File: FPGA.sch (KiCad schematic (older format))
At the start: 56 parts, among them J1 Conn_02x07_Odd_Even, J2 26642801RP2, U3 XC7A100T-FTG256, U4 S25FL1, U5 SiT2024B, U6 AS6C1616

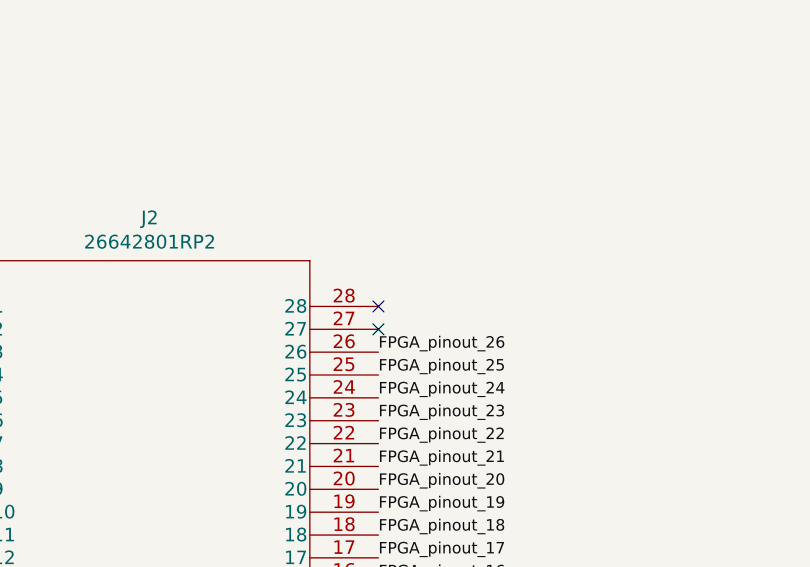
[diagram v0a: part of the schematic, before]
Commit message: Partially route FPGA
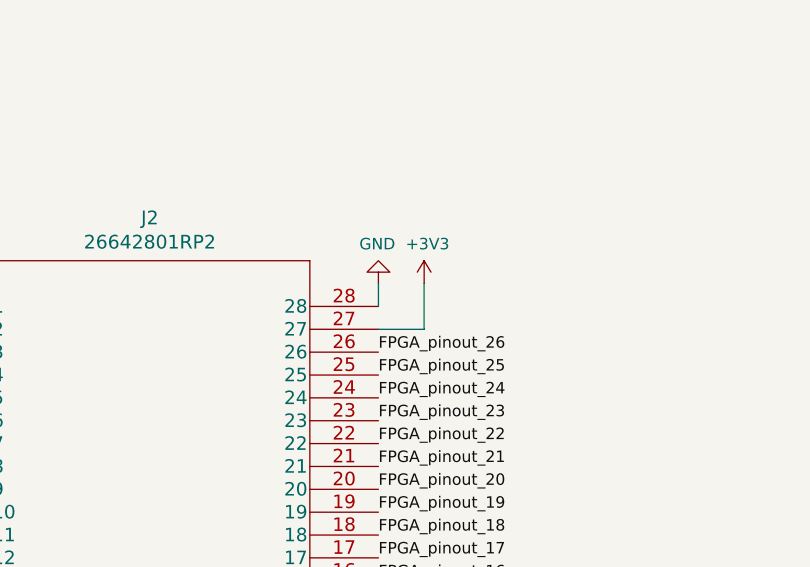
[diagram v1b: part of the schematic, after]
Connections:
- net +3V3: now also J2.27
- net GND: now also J2.28
- no-connect marks 90 -> 88
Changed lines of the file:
@@
 Text Label 5850 9000 0    50   ~ 0
 FPGA_pinout_26
-NoConn ~ 5850 8800
-NoConn ~ 5850 8900
 Wire Wire Line
 	5400 4000 6900 4000
@@
 Text Notes -400 7450 2    50   ~ 0
 Vccint
+$Comp
+L power:GND #PWR0172
+U 1 1 5D9DC146
+P 5850 8700
+F 0 "#PWR0172" H 5850 8450 50  0001 C CNN
+F 1 "GND" H 5855 8527 50  0000 C CNN
+F 2 "" H 5850 8700 50  0001 C CNN
+F 3 "" H 5850 8700 50  0001 C CNN
+	1    5850 8700
+	-1   0    0    1
+$EndComp
+$Comp
+L power:+3V3 #PWR0181
+U 1 1 5D9DC78C
+P 6050 8700
+F 0 "#PWR0181" H 6050 8550 50  0001 C CNN
+F 1 "+3V3" H 6065 8873 50  0000 C CNN
+F 2 "" H 6050 8700 50  0001 C CNN
+F 3 "" H 6050 8700 50  0001 C CNN
+	1    6050 8700
+	1    0    0    -1
+$EndComp
+Wire Wire Line
+	5850 8800 5850 8700
+Wire Wire Line
+	6050 8700 6050 8900
+Wire Wire Line
+	6050 8900 5850 8900
 $EndSCHEMATC

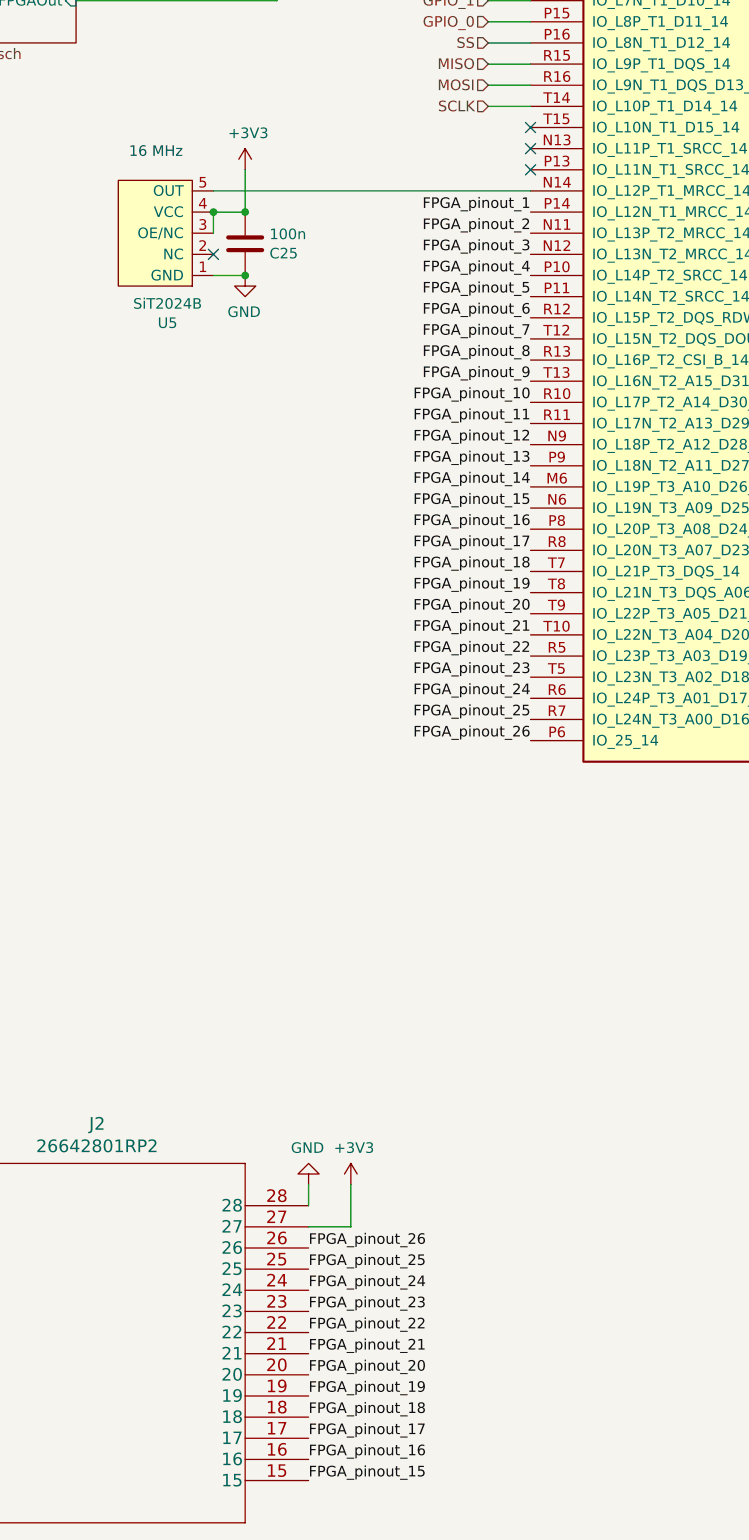
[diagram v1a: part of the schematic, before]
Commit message: Partially route FPGA pinout
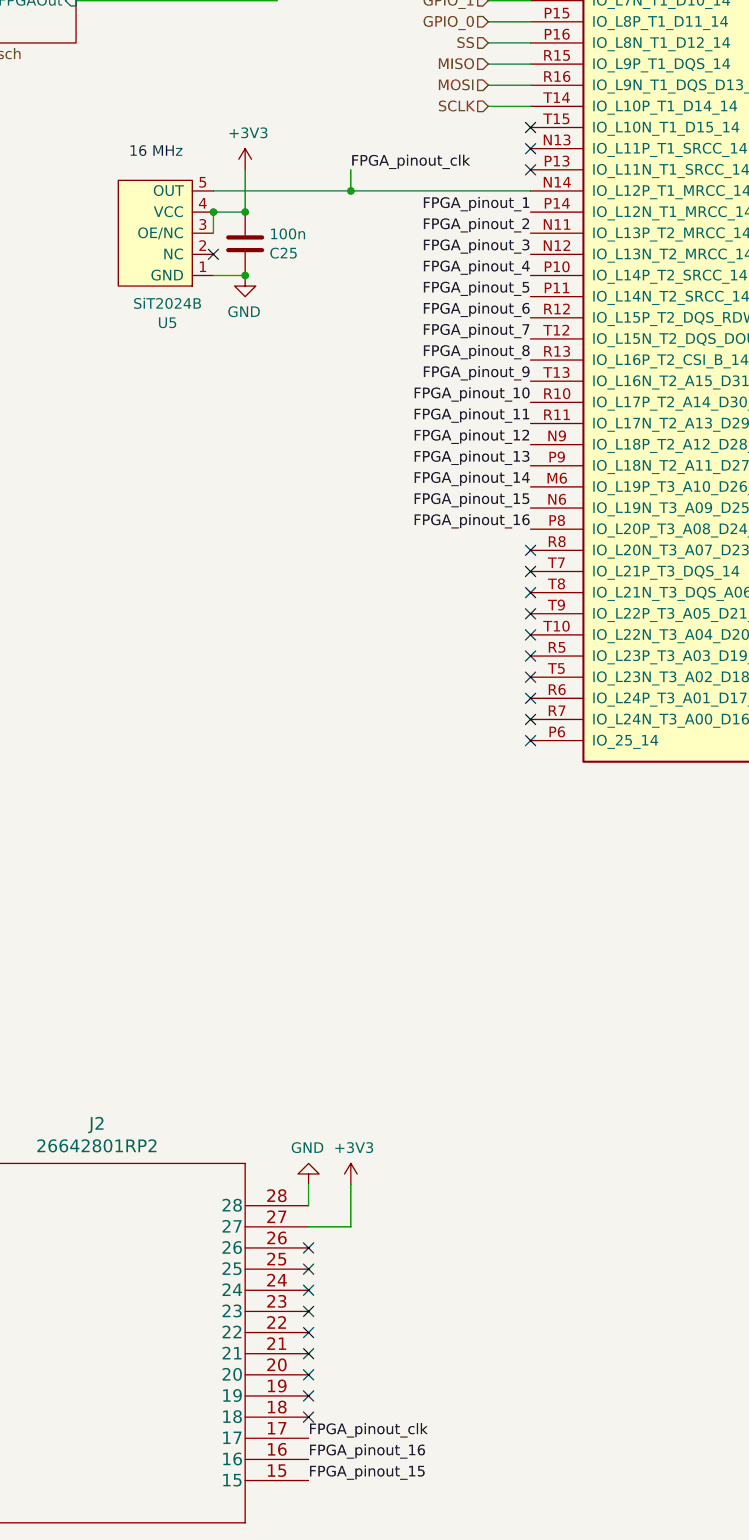
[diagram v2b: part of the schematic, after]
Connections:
- net FPGA_pinout_clk: now reaches U3.N14 (IO_L12P_T1_MRCC_14), U5.5 (OUT)
- net FPGA_pinout_clk: now also J2.17
- net FPGA_pinout_17: no longer names the net of U3.R8 (IO_L20N_T3_A07_D23_14)
- net FPGA_pinout_17: no longer J2.17
- net FPGA_pinout_18: no longer names the net of U3.T7 (IO_L21P_T3_DQS_14)
- net FPGA_pinout_18: no longer J2.18
- net FPGA_pinout_19: no longer names the net of U3.T8 (IO_L21N_T3_DQS_A06_D22_14)
- net FPGA_pinout_19: no longer J2.19
- net FPGA_pinout_20: no longer names the net of U3.T9 (IO_L22P_T3_A05_D21_14)
- net FPGA_pinout_20: no longer J2.20
- net FPGA_pinout_21: no longer names the net of U3.T10 (IO_L22N_T3_A04_D20_14)
- net FPGA_pinout_21: no longer J2.21
- net FPGA_pinout_22: no longer names the net of U3.R5 (IO_L23P_T3_A03_D19_14)
- net FPGA_pinout_22: no longer J2.22
- net FPGA_pinout_23: no longer names the net of U3.T5 (IO_L23N_T3_A02_D18_14)
- net FPGA_pinout_23: no longer J2.23
- net FPGA_pinout_24: no longer names the net of U3.R6 (IO_L24P_T3_A01_D17_14)
- net FPGA_pinout_24: no longer J2.24
- net FPGA_pinout_25: no longer names the net of U3.R7 (IO_L24N_T3_A00_D16_14)
- net FPGA_pinout_25: no longer J2.25
- net FPGA_pinout_26: no longer names the net of U3.P6 (IO_25_14)
- net FPGA_pinout_26: no longer J2.26
- no-connect marks 88 -> 107
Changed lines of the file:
@@
 Wire Wire Line
 	6900 3200 6700 3200
-$Comp
-L pin_header:26642801RP2 J2
-U 1 1 5F44891F
-P 3850 8800
-F 0 "J2" H 4850 9187 60  0000 C CNN
-F 1 "26642801RP2" H 4850 9081 60  0000 C CNN
-F 2 "Connector_PinHeader_2.54mm:PinHeader_2x14_P2.54mm_Vertical" H 4850 9040 60  0001 C CNN
-F 3 "" H 3850 8800 60  0000 C CNN
-	1    3850 8800
-	1    0    0    -1
-$EndComp
 Text Label 6900 4100 2    50   ~ 0
 FPGA_pinout_1
@@
 Text Label 6900 5600 2    50   ~ 0
 FPGA_pinout_16
-Text Label 6900 5700 2    50   ~ 0
-FPGA_pinout_17
-Text Label 6900 5800 2    50   ~ 0
-FPGA_pinout_18
-Text Label 6900 5900 2    50   ~ 0
-FPGA_pinout_19
-Text Label 6900 6000 2    50   ~ 0
-FPGA_pinout_20
-Text Label 6900 6100 2    50   ~ 0
-FPGA_pinout_21
-Text Label 6900 6200 2    50   ~ 0
-FPGA_pinout_22
-Text Label 6900 6300 2    50   ~ 0
-FPGA_pinout_23
-Text Label 6900 6400 2    50   ~ 0
-FPGA_pinout_24
-Text Label 6900 6500 2    50   ~ 0
-FPGA_pinout_25
-Text Label 6900 6600 2    50   ~ 0
-FPGA_pinout_26
-Text Label 3850 8800 2    50   ~ 0
-FPGA_pinout_1
-Text Label 3850 8900 2    50   ~ 0
-FPGA_pinout_2
-Text Label 3850 9000 2    50   ~ 0
-FPGA_pinout_3
-Text Label 3850 9100 2    50   ~ 0
-FPGA_pinout_4
-Text Label 3850 9200 2    50   ~ 0
-FPGA_pinout_5
-Text Label 3850 9300 2    50   ~ 0
-FPGA_pinout_6
-Text Label 3850 9400 2    50   ~ 0
-FPGA_pinout_7
-Text Label 3850 9500 2    50   ~ 0
-FPGA_pinout_8
-Text Label 3850 9600 2    50   ~ 0
-FPGA_pinout_9
-Text Label 3850 9700 2    50   ~ 0
-FPGA_pinout_10
-Text Label 3850 9800 2    50   ~ 0
-FPGA_pinout_11
-Text Label 3850 9900 2    50   ~ 0
-FPGA_pinout_12
-Text Label 3850 10000 2    50   ~ 0
-FPGA_pinout_13
-Text Label 3850 10100 2    50   ~ 0
-FPGA_pinout_14
-Text Label 5850 10100 0    50   ~ 0
-FPGA_pinout_15
-Text Label 5850 10000 0    50   ~ 0
-FPGA_pinout_16
-Text Label 5850 9900 0    50   ~ 0
-FPGA_pinout_17
-Text Label 5850 9800 0    50   ~ 0
-FPGA_pinout_18
-Text Label 5850 9700 0    50   ~ 0
-FPGA_pinout_19
-Text Label 5850 9600 0    50   ~ 0
-FPGA_pinout_20
-Text Label 5850 9500 0    50   ~ 0
-FPGA_pinout_21
-Text Label 5850 9400 0    50   ~ 0
-FPGA_pinout_22
-Text Label 5850 9300 0    50   ~ 0
-FPGA_pinout_23
-Text Label 5850 9200 0    50   ~ 0
-FPGA_pinout_24
-Text Label 5850 9100 0    50   ~ 0
-FPGA_pinout_25
-Text Label 5850 9000 0    50   ~ 0
-FPGA_pinout_26
-Wire Wire Line
-	5400 4000 6900 4000
+Wire Wire Line
+	5400 4000 6050 4000
 Text Notes -300 6200 2    50   ~ 0
 Vccbram
@@
 Text Notes -400 7450 2    50   ~ 0
 Vccint
+Wire Wire Line
+	6050 8900 5850 8900
+Wire Wire Line
+	6050 8700 6050 8900
+Wire Wire Line
+	5850 8800 5850 8700
+$Comp
+L power:+3V3 #PWR0181
+U 1 1 5D9DC78C
+P 6050 8700
+F 0 "#PWR0181" H 6050 8550 50  0001 C CNN
+F 1 "+3V3" H 6065 8873 50  0000 C CNN
+F 2 "" H 6050 8700 50  0001 C CNN
+F 3 "" H 6050 8700 50  0001 C CNN
+	1    6050 8700
+	1    0    0    -1
+$EndComp
 $Comp
 L power:GND #PWR0172
@@
 $EndComp
 $Comp
-L power:+3V3 #PWR0181
-U 1 1 5D9DC78C
-P 6050 8700
-F 0 "#PWR0181" H 6050 8550 50  0001 C CNN
-F 1 "+3V3" H 6065 8873 50  0000 C CNN
-F 2 "" H 6050 8700 50  0001 C CNN
-F 3 "" H 6050 8700 50  0001 C CNN
-	1    6050 8700
+L pin_header:26642801RP2 J2
+U 1 1 5F44891F
+P 3850 8800
+F 0 "J2" H 4850 9187 60  0000 C CNN
+F 1 "26642801RP2" H 4850 9081 60  0000 C CNN
+F 2 "Connector_PinHeader_2.54mm:PinHeader_2x14_P2.54mm_Vertical" H 4850 9040 60  0001 C CNN
+F 3 "" H 3850 8800 60  0000 C CNN
+	1    3850 8800
 	1    0    0    -1
 $EndComp
-Wire Wire Line
-	5850 8800 5850 8700
-Wire Wire Line
-	6050 8700 6050 8900
-Wire Wire Line
-	6050 8900 5850 8900
+Text Label 3850 9500 2    50   ~ 0
+FPGA_pinout_8
+Text Label 3850 9400 2    50   ~ 0
+FPGA_pinout_7
+Text Label 3850 9300 2    50   ~ 0
+FPGA_pinout_6
+Text Label 3850 9200 2    50   ~ 0
+FPGA_pinout_5
+Text Label 3850 9100 2    50   ~ 0
+FPGA_pinout_4
+Text Label 3850 9000 2    50   ~ 0
+FPGA_pinout_3
+Text Label 3850 8900 2    50   ~ 0
+FPGA_pinout_2
+Text Label 3850 8800 2    50   ~ 0
+FPGA_pinout_1
+Text Label 3850 10100 2    50   ~ 0
+FPGA_pinout_14
+Text Label 3850 10000 2    50   ~ 0
+FPGA_pinout_13
+Text Label 3850 9900 2    50   ~ 0
+FPGA_pinout_12
+Text Label 3850 9800 2    50   ~ 0
+FPGA_pinout_11
+Text Label 3850 9700 2    50   ~ 0
+FPGA_pinout_10
+Text Label 3850 9600 2    50   ~ 0
+FPGA_pinout_9
+Text Label 5850 10000 0    50   ~ 0
+FPGA_pinout_16
+Text Label 5850 10100 0    50   ~ 0
+FPGA_pinout_15
+Text Label 5850 9900 0    50   ~ 0
+FPGA_pinout_clk
+NoConn ~ 5850 9000
+NoConn ~ 5850 9100
+NoConn ~ 5850 9200
+NoConn ~ 5850 9300
+NoConn ~ 5850 9400
+NoConn ~ 5850 9500
+NoConn ~ 5850 9600
+NoConn ~ 5850 9700
+NoConn ~ 5850 9800
+NoConn ~ 6900 5700
+NoConn ~ 6900 5800
+NoConn ~ 6900 5900
+NoConn ~ 6900 6000
+NoConn ~ 6900 6100
+NoConn ~ 6900 6200
+NoConn ~ 6900 6300
+NoConn ~ 6900 6400
+NoConn ~ 6900 6500
+NoConn ~ 6900 6600
+Text Label 6050 3900 0    50   ~ 0
+FPGA_pinout_clk
+Wire Wire Line
+	6050 3900 6050 4000
+Connection ~ 6050 4000
+Wire Wire Line
+	6050 4000 6900 4000
 $EndSCHEMATC

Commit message: Finish PCB wiring
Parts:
- removed C48: 47u, Capacitor_SMD:C_1206_3216Metric_Pad1.42x1.75mm_HandSolder, symbol Device:C
- removed C50, C52: 4.7u, Capacitor_SMD:C_1206_3216Metric_Pad1.42x1.75mm_HandSolder, symbol Device:C
- removed C54, C56, C58, C60: 0.47u, Capacitor_SMD:C_1206_3216Metric_Pad1.42x1.75mm_HandSolder, symbol Device:C
- removed C63: 100n, Capacitor_SMD:C_1206_3216Metric_Pad1.42x1.75mm_HandSolder, symbol Device:C
- removed U6: AS6C1616, Package_SO:TSOP-I-48_18.4x12mm_P0.5mm, symbol Memory_RAM:AS6C1616
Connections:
- net +3V3: no longer U3.A6 (VCCO_35), U3.B3 (VCCO_35), U3.D7 (VCCO_35), U3.E4 (VCCO_35), U3.F1 (VCCO_35), U3.J2 (VCCO_35)
- net GND: now also U3.A6 (VCCO_35), U3.B3 (VCCO_35), U3.D7 (VCCO_35), U3.E4 (VCCO_35), U3.F1 (VCCO_35), U3.J2 (VCCO_35)
- net FPGA_pinout_clk: no longer names the net of U3.N14 (IO_L12P_T1_MRCC_14), U5.5 (OUT)
- net FPGA_pinout_clk: no longer J2.17
- net SRAM_a0: no longer names the net of U3.A2 (IO_L8N_T1_AD14N_35)
- net SRAM_a1: no longer names the net of U3.C1 (IO_L9P_T1_DQS_AD7P_35)
- net SRAM_a10: no longer names the net of U3.E5 (IO_L13N_T2_MRCC_35)
- net SRAM_a11: no longer names the net of U3.F4 (IO_L14P_T2_SRCC_35)
- net SRAM_a12: no longer names the net of U3.F3 (IO_L14N_T2_SRCC_35)
- net SRAM_a13: no longer names the net of U3.F2 (IO_L15P_T2_DQS_35)
- net SRAM_a14: no longer names the net of U3.E1 (IO_L15N_T2_DQS_35)
- net SRAM_a15: no longer names the net of U3.G5 (IO_L16P_T2_35)
- net SRAM_a16: no longer names the net of U3.G4 (IO_L16N_T2_35)
- net SRAM_a17: no longer names the net of U3.G2 (IO_L17P_T2_35)
- net SRAM_a18: no longer names the net of U3.G1 (IO_L17N_T2_35)
- net SRAM_a19: no longer names the net of U3.H5 (IO_L18P_T2_35)
- net SRAM_a2: no longer names the net of U3.B1 (IO_L9N_T1_DQS_AD7N_35)
- net SRAM_a3: no longer names the net of U3.E2 (IO_L10P_T1_AD15P_35)
- net SRAM_a4: no longer names the net of U3.D1 (IO_L10N_T1_AD15N_35)
- net SRAM_a5: no longer names the net of U3.E3 (IO_L11P_T1_SRCC_35)
- net SRAM_a6: no longer names the net of U3.D3 (IO_L11N_T1_SRCC_35)
- net SRAM_a7: no longer names the net of U3.D4 (IO_L12P_T1_MRCC_35)
- net SRAM_a8: no longer names the net of U3.C4 (IO_L12N_T1_MRCC_35)
- net SRAM_a9: no longer names the net of U3.F5 (IO_L13P_T2_MRCC_35)
- net SRAM_ce#: no longer names the net of U3.J4 (IO_L19N_T3_VREF_35)
- net SRAM_ce2: no longer names the net of U3.H2 (IO_L20P_T3_35)
- net SRAM_dio0: no longer names the net of U3.E6 (IO_0_35)
- net SRAM_dio1: no longer names the net of U3.B7 (IO_L1P_T0_AD4P_35)
- net SRAM_dio10: no longer names the net of U3.C6 (IO_L5N_T0_AD13N_35)
- net SRAM_dio11: no longer names the net of U3.D6 (IO_L6P_T0_35)
- net SRAM_dio12: no longer names the net of U3.D5 (IO_L6N_T0_VREF_35)
- net SRAM_dio13: no longer names the net of U3.C3 (IO_L7P_T1_AD6P_35)
- net SRAM_dio14: no longer names the net of U3.C2 (IO_L7N_T1_AD6N_35)
- net SRAM_dio15: no longer names the net of U3.B2 (IO_L8P_T1_AD14P_35)
- net SRAM_dio2: no longer names the net of U3.A7 (IO_L1N_T0_AD4N_35)
- net SRAM_dio3: no longer names the net of U3.B6 (IO_L2P_T0_AD12P_35)
- net SRAM_dio4: no longer names the net of U3.B5 (IO_L2N_T0_AD12N_35)
- net SRAM_dio5: no longer names the net of U3.A5 (IO_L3P_T0_DQS_AD5P_35)
- net SRAM_dio6: no longer names the net of U3.A4 (IO_L3N_T0_DQS_AD5N_35)
- net SRAM_dio7: no longer names the net of U3.B4 (IO_L4P_T0_35)
- net SRAM_dio8: no longer names the net of U3.A3 (IO_L4N_T0_35)
- net SRAM_dio9: no longer names the net of U3.C7 (IO_L5P_T0_AD13P_35)
- net SRAM_lb#: no longer names the net of U3.J3 (IO_L21P_T3_DQS_35)
- net SRAM_oe#: no longer names the net of U3.H4 (IO_L18N_T2_35)
- net SRAM_ub#: no longer names the net of U3.H1 (IO_L20N_T3_35)
- net SRAM_we#: no longer names the net of U3.J5 (IO_L19P_T3_35)
- no-connect marks 107 -> 150
